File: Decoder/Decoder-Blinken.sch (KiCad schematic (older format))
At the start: 52 parts, among them U941 74LS04, U942 74LS04, U943 74LS04, U944 74LS04

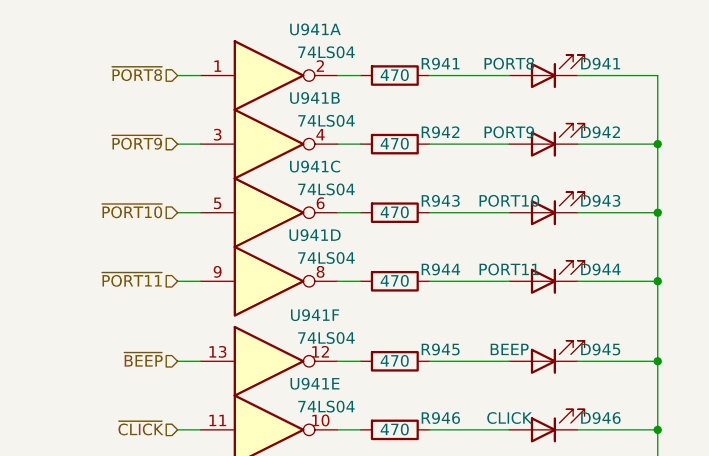
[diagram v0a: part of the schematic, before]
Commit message: Schematics for display & keyboard, adding LEDs to processor PCB
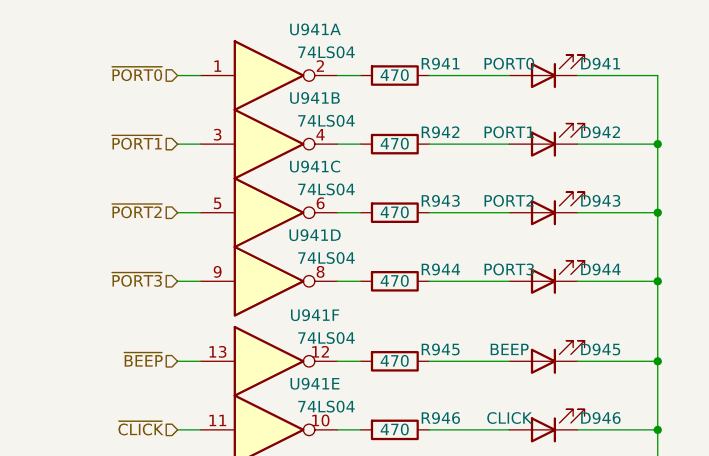
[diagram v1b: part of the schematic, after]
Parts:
- D941: value PORT8 -> PORT0
- D942: value PORT9 -> PORT1
- D943: value PORT10 -> PORT2
- D944: value PORT11 -> PORT3
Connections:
- net ~PORT10 renamed ~PORT2
- net ~PORT11 renamed ~PORT3
- net ~PORT8 renamed ~PORT0
- net ~PORT9 renamed ~PORT1
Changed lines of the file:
@@
 ~COM4
 Text HLabel 1800 1450 0    50   Input ~ 0
-~PORT8
+~PORT0
 Text HLabel 1800 1750 0    50   Input ~ 0
-~PORT9
+~PORT1
 Text HLabel 1800 2050 0    50   Input ~ 0
-~PORT10
+~PORT2
 Text HLabel 1800 2350 0    50   Input ~ 0
-~PORT11
+~PORT3
 Text HLabel 1800 2700 0    50   Input ~ 0
 ~BEEP
@@
 AR Path="/628221FF/63B61FD8/63B81296" Ref="D944"  Part="1"
 F 0 "D944" H 3150 2300 50  0000 C CNN
-F 1 "PORT11" H 3550 2300 50  0000 C CNN
+F 1 "PORT3" H 3550 2300 50  0000 C CNN
 F 2 "Datapoint2200:LED_Dialight_597_xxxx_407F_SMT_RA_3mmx2mmx1mm" H 3400 2350 50  0001 C CNN
 F 3 "~" H 3400 2350 50  0001 C CNN
@@
 AR Path="/628221FF/63B61FD8/63B81290" Ref="D943"  Part="1"
 F 0 "D943" H 3150 2000 50  0000 C CNN
-F 1 "PORT10" H 3550 2000 50  0000 C CNN
+F 1 "PORT2" H 3550 2000 50  0000 C CNN
 F 2 "Datapoint2200:LED_Dialight_597_xxxx_407F_SMT_RA_3mmx2mmx1mm" H 3400 2050 50  0001 C CNN
 F 3 "~" H 3400 2050 50  0001 C CNN
@@
 AR Path="/628221FF/63B61FD8/63B8128A" Ref="D942"  Part="1"
 F 0 "D942" H 3150 1700 50  0000 C CNN
-F 1 "PORT9" H 3550 1700 50  0000 C CNN
+F 1 "PORT1" H 3550 1700 50  0000 C CNN
 F 2 "Datapoint2200:LED_Dialight_597_xxxx_407F_SMT_RA_3mmx2mmx1mm" H 3400 1750 50  0001 C CNN
 F 3 "~" H 3400 1750 50  0001 C CNN
@@
 AR Path="/628221FF/63B61FD8/63B81284" Ref="D941"  Part="1"
 F 0 "D941" H 3150 1400 50  0000 C CNN
-F 1 "PORT8" H 3550 1400 50  0000 C CNN
+F 1 "PORT0" H 3550 1400 50  0000 C CNN
 F 2 "Datapoint2200:LED_Dialight_597_xxxx_407F_SMT_RA_3mmx2mmx1mm" H 3400 1450 50  0001 C CNN
 F 3 "~" H 3400 1450 50  0001 C CNN
